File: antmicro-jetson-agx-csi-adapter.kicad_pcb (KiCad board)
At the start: 4 copper layers, 73.6 x 41 mm, 102 parts, among them IC1 MAX1708EEE+, J1 QTH-060-03-L-D-A, J2 WE_68715014522_ONE-SIDE, J3 SM06B-SRSS-TB(LF)(SN), J4 WE_68715014022, J5 SM09B-SRSS-TB(LF)(SN), J6 61300611121, Q1 BSS138AKA, U1 NTS0102DP, U2 PCA9547BS,118, U3 BNO055

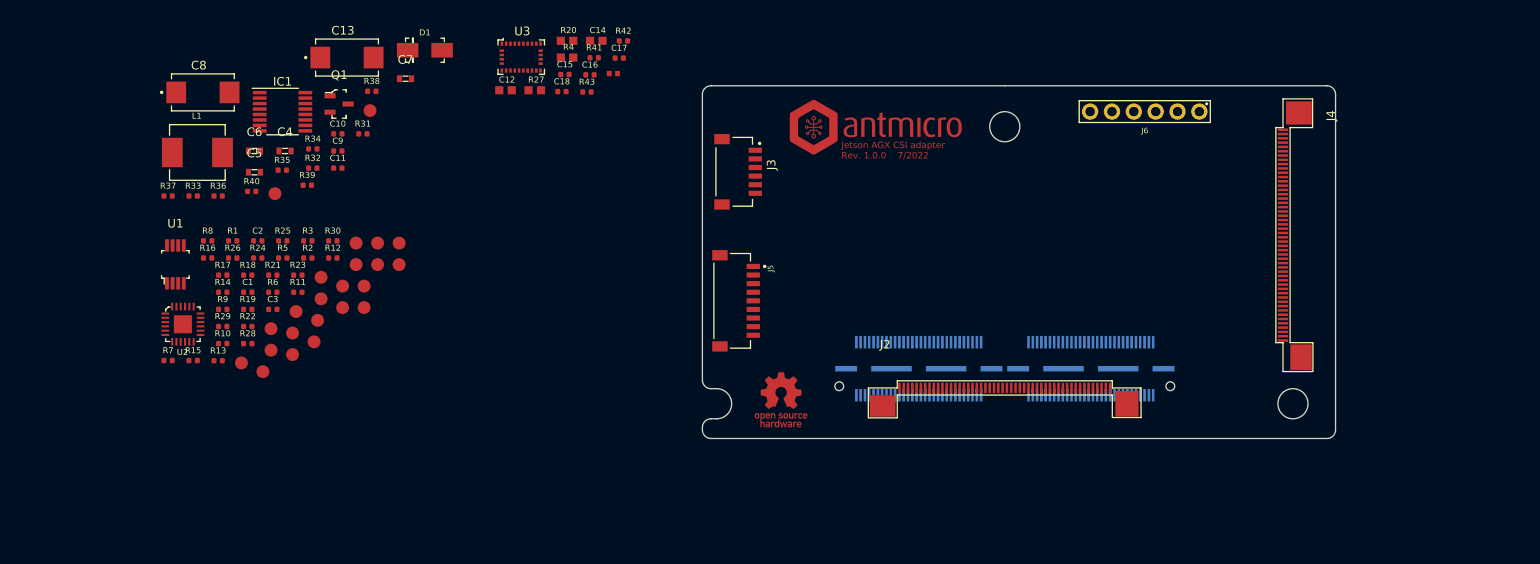
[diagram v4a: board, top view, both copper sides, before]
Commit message: Routed CSI interface
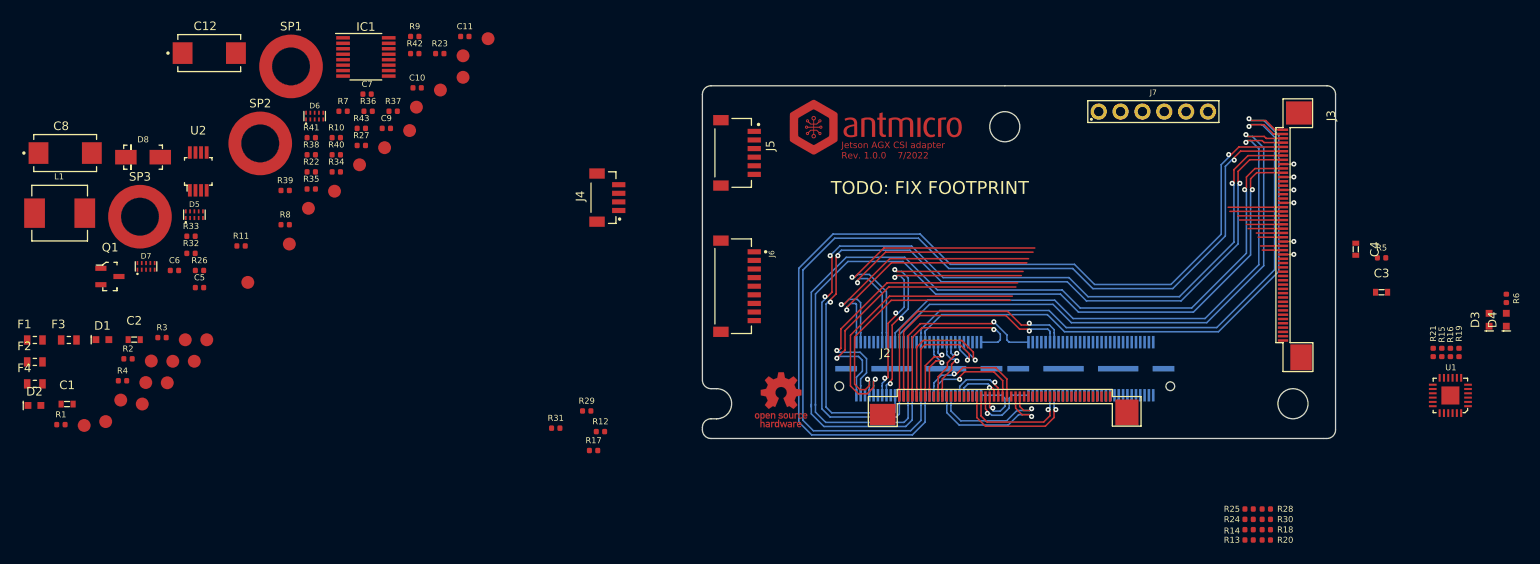
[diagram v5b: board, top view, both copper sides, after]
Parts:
- removed C13: C_220u_KEMET_D, antmicro-footprints:KEMET_D
- removed C14: 100n, antmicro-footprints:0603
- removed C15: C_10n_0402, antmicro-footprints:0402-cap
- removed C16, C17, C18: C_100n_0402, antmicro-footprints:0402-cap
- removed C19: 100n, antmicro-footprints:0402
- removed the J3 at (121.0, 78.0)
- removed U3: BNO055, antmicro-footprints:LGA-28_5.2x3.8mm_BNO0055
- added D2: LTST-C190GKT, antmicro-footprints:LED_0603, F.Cu at (37.2, 105.2)
- added D3: LTST-C190GKT, antmicro-footprints:LED_0603, F.Cu at (206.3, 95.2)
- added D4: LTST-C190GKT, antmicro-footprints:LED_0603, F.Cu at (208.3, 95.2)
- added D5: PUSB3F96X_PASS, antmicro-footprints:PUSB3F96X, F.Cu at (55.8, 83.0)
- added D6: PUSB3F96X_PASS, antmicro-footprints:PUSB3F96X, F.Cu at (69.8, 71.5)
- added D7: PUSB3F96X_PASS, antmicro-footprints:PUSB3F96X, F.Cu at (50.2, 89.0)
- added D8: B340A-13-F, antmicro-footprints:DO-214AC, F.Cu at (49.8, 76.3)
- added F1: 04671.25NR, antmicro-footprints:0603-Fuse-Littelfuse-0467, F.Cu at (37.2, 97.5)
- added F2: 04671.25NR, antmicro-footprints:0603-Fuse-Littelfuse-0467, F.Cu at (37.2, 100.1)
- added F3: 04671.25NR, antmicro-footprints:0603-Fuse-Littelfuse-0467, F.Cu at (41.2, 97.5)
- added F4: 04671.25NR, antmicro-footprints:0603-Fuse-Littelfuse-0467, F.Cu at (37.2, 102.7)
- added J4: BM04B-SRSS-TB-LF-SN, antmicro-footprints:BM04B-SRSS-TB-LF-SN, F.Cu at (103.8, 81.0)
- added J7: 61300611121, antmicro-footprints:61300611121, F.Cu at (167.3, 71.0)
- added SP1: 9774110360, antmicro-footprints:Mounting_Wuerth_WA-SMSI-M3_H11mm_9774110360, F.Cu at (67.0, 65.8)
- added SP2: 9774110360, antmicro-footprints:Mounting_Wuerth_WA-SMSI-M3_H11mm_9774110360, F.Cu at (63.5, 74.7)
- added SP3: 9774110360, antmicro-footprints:Mounting_Wuerth_WA-SMSI-M3_H11mm_9774110360, F.Cu at (49.5, 83.2)
- C1, C2, C3: value C_100n_0402 -> C_1u_0603; footprint antmicro-footprints:0402-cap -> antmicro-footprints:0603-cap
- C12: value 100n -> C_220u_KEMET_D; footprint antmicro-footprints:0603 -> antmicro-footprints:KEMET_D
- C5, C6, C7: value C_1u_0603 -> C_100n_0402; footprint antmicro-footprints:0603-cap -> antmicro-footprints:0402-cap
- D1: value B340A-13-F -> LTST-C190GKT; footprint antmicro-footprints:DO-214AC -> antmicro-footprints:LED_0603
- J5: value SM09B-SRSS-TB(LF)(SN) -> SM06B-SRSS-TB(LF)(SN); footprint antmicro-footprints:JST_SM09B-SRSS-TB(LF)(SN) -> antmicro-footprints:JST_SM06B-SRSS-TB(LF)(SN)
- J6: value 61300611121 -> SM09B-SRSS-TB(LF)(SN); footprint antmicro-footprints:61300611121 -> antmicro-footprints:JST_SM09B-SRSS-TB(LF)(SN)
- R10, R26, R37, R39, R9: value R_2k_0402 -> R_0R_0402
- R11: value R_0R_0402 -> R_10k_0402
- R12, R33, R34, R35: value R_0R_0402 -> R_2k_0402
- R15, R16: value R_2k2_0402 -> R_0R_0402
- R20: value 2k2 -> R_2k_0402; footprint antmicro-footprints:0603 -> antmicro-footprints:0402-res
- R22, R23: value R_0R_0402 -> R_2k2_0402
- R27: value 0R -> R_0R_0402; footprint antmicro-footprints:0603 -> antmicro-footprints:0402-res
- R3, R5: value R_0R_0402 -> R_200R_0402
- R38: value R_2R_0402 -> R_0R_0402
- R4: value 0R -> R_470R_0402; footprint antmicro-footprints:0603 -> antmicro-footprints:0402-res
- R40: value R_0R_0402 -> R_2R_0402
- R41, R43: value R_10k_0402 -> R_2k_0402
- R6: value R_0R_0402 -> R_470R_0402
- R8: value R_10k_0402 -> R_0R_0402
- U1: value NTS0102DP -> PCA9547BS,118; footprint antmicro-footprints:TSSOP-8_W3mm -> antmicro-footprints:HVQFN24
- U2: value PCA9547BS,118 -> NTS0102DP; footprint antmicro-footprints:HVQFN24 -> antmicro-footprints:TSSOP-8_W3mm
- moved U1 149.0 mm to (201.8, 104.0), turned to 180 degrees
- moved R15 145.2 mm to (200.8, 99.0), turned to -90 degrees
- moved R16 144.9 mm to (201.8, 99.0), turned to -90 degrees
- moved R6 143.4 mm to (208.3, 92.7), turned to -90 degrees
- moved R19 140.9 mm to (202.8, 99.0), turned to 90 degrees
- moved R21 135.2 mm to (199.8, 99.0), turned to 90 degrees
- moved C3 128.9 mm to (193.8, 92.0)
- moved R5 127.7 mm to (193.8, 88.0)
- moved C4 125.0 mm to (190.8, 87.0), turned to -90 degrees
- moved R14 122.5 mm to (178.4, 119.6)
- moved R18 122.0 mm to (180.4, 119.6)
- moved R13 121.6 mm to (178.4, 120.8)
- moved R28 120.0 mm to (180.4, 117.2)
- moved R24 119.2 mm to (178.4, 118.4)
- moved R25 116.6 mm to (178.4, 117.2)
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- renumbered J4 to J3
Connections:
- net /Cameras/CAM1_RST_3V3 renamed /Interface/CAM1_RST_3V3
- net /Cameras/CAM_RST_3V3 renamed /Interface/CAM_RST_3V3
- net CSI0_D1_N renamed /Interface/CSI0_D1_N
- net CSI0_D1_P renamed /Interface/CSI0_D1_P
- net CSI1_CLK_N renamed /Interface/CSI1_CLK_N
- net CSI1_D1_N renamed /Interface/CSI1_D1_N
- net CSI1_D1_P renamed /Interface/CSI1_D1_P
- net CSI2_CLK_N renamed /Interface/CSI2_CLK_N
- net CSI2_CLK_P renamed /Interface/CSI2_CLK_P
- net CSI2_D0_N renamed /Interface/CSI2_D0_N
- net CSI2_D0_P renamed /Interface/CSI2_D0_P
- net CSI2_D1_N renamed /Interface/CSI2_D1_N
- net CSI2_D1_P renamed /Interface/CSI2_D1_P
- net CSI3_CLK_N renamed /Interface/CSI3_CLK_N
- net CSI3_CLK_P renamed /Interface/CSI3_CLK_P
- net CSI3_D0_N renamed /Interface/CSI3_D0_N
- net CSI3_D0_P renamed /Interface/CSI3_D0_P
- net CSI3_D1_N renamed /Interface/CSI3_D1_N
- net CSI3_D1_P renamed /Interface/CSI3_D1_P
- net CSI4_D0_N renamed /Interface/CSI4_D0_N
- net CSI4_D0_P renamed /Interface/CSI4_D0_P
- net CSI4_D1_N renamed /Interface/CSI4_D1_N
- net CSI4_D1_P renamed /Interface/CSI4_D1_P
- net CSI5_CLK_N renamed /Interface/CSI5_CLK_N
- net CSI5_CLK_P renamed /Interface/CSI5_CLK_P
- net CSI5_D0_N renamed /Interface/CSI5_D0_N
- net CSI5_D0_P renamed /Interface/CSI5_D0_P
- net CSI5_D1_N renamed /Interface/CSI5_D1_N
- net CSI5_D1_P renamed /Interface/CSI5_D1_P
- net CSI6_CLK_N renamed /Interface/CSI6_CLK_N
- net CSI6_CLK_P renamed /Interface/CSI6_CLK_P
- net CSI6_D0_N renamed /Interface/CSI6_D0_N
- net CSI6_D0_P renamed /Interface/CSI6_D0_P
- net CSI6_D1_N renamed /Interface/CSI6_D1_N
- net CSI6_D1_P renamed /Interface/CSI6_D1_P
- net CSI7_CLK_N renamed /Interface/CSI7_CLK_N
- net CSI7_CLK_P renamed /Interface/CSI7_CLK_P
- net CSI7_D0_N renamed /Interface/CSI7_D0_N
- net CSI7_D0_P renamed /Interface/CSI7_D0_P
- net CSI7_D1_N renamed /Interface/CSI7_D1_N
- net CSI7_D1_P renamed /Interface/CSI7_D1_P
- C1 pad 1: +1V8 -> Net-(C1-Pad1)
- C12 pad 1: GND -> Net-(C12-Pad1)
- C12 pad 2: 3V3 -> GND
- C2 pad 1: +3V3 -> Net-(C2-Pad1)
- C3 pad 1: +3V3 -> Net-(C3-Pad1)
- C4 pad 1: +5V -> Net-(C4-Pad1)
- C6 pad 1: +5V -> +1V8
- IC1 pad 3: Net-(D1-PadA) -> Net-(D8-PadA)
- IC1 pad 4: Net-(D1-PadA) -> Net-(D8-PadA)
- IC1 pad 5: Net-(D1-PadA) -> Net-(D8-PadA)
- J1 pad 43: CSI4_CLK_P -> /Interface/CSI4_CLK_P
- J1 pad 45: CSI4_CLK_N -> /Interface/CSI4_CLK_N
- J1 pad 75: /Interface/I2C_GP3_CLK -> I2C_GP3_CLK
- J1 pad 77: /Interface/I2C_GP3_DAT -> I2C_GP3_DAT
- J2 pad 28: CSI4_CLK_N -> /Interface/CSI4_CLK_P
- J2 pad 29: CSI4_CLK_P -> /Interface/CSI4_CLK_N
- J2 pad 32: /Cameras/VSYNC_CAM0_3V3 -> /Interface/VSYNC_CAM0_3V3
- J2 pad 34: /Cameras/VSYNC_CAM1_3V3 -> /Interface/VSYNC_CAM1_3V3
- J2 pad 47: +3V3 -> Net-(C1-Pad1)
- J2 pad 48: +3V3 -> Net-(C1-Pad1)
- J2 pad 49: +5V -> Net-(C2-Pad1)
- J2 pad 50: +5V -> Net-(C2-Pad1)
- J3 pad 21: CSI1_D0_N -> /Interface/CSI1_D0_N
- J3 pad 22: CSI1_D0_P -> /Interface/CSI1_D0_P
- J3 pad 25: CSI0_D0_N -> /Interface/CSI0_D0_N
- J3 pad 26: CSI0_D0_P -> /Interface/CSI0_D0_P
- J3 pad 28: CSI0_CLK_N -> /Interface/CSI0_CLK_N
- J3 pad 29: CSI0_CLK_P -> /Interface/CSI0_CLK_P
- J3 pad 32: /Cameras/VSYNC_CAM3_3V3 -> /Interface/VSYNC_CAM3_3V3
- J3 pad 34: /Cameras/VSYNC_CAM2_3V3 -> /Interface/VSYNC_CAM2_3V3
- J3 pad 47: +3V3 -> Net-(C3-Pad1)
- J3 pad 48: +3V3 -> Net-(C3-Pad1)
- J3 pad 49: +5V -> Net-(C4-Pad1)
- J3 pad 50: +5V -> Net-(C4-Pad1)
- J5 pad 1: /Cameras/GPIO3 -> +5V
- J5 pad 2: /Cameras/GPIO4 -> GND
- J5 pad 3: /Cameras/GPIO5 -> CAM3_SDA
- J5 pad 4: /Cameras/GPIO6 -> CAM3_SCL
- J5 pad 5: /Cameras/DEPTH_CAM_SYNC -> unconnected-(J5-Pad5)
- J5 pad 6: /Cameras/LASER_PWM0 -> unconnected-(J5-Pad6)
- J6 pad 1: GND -> /Auxiliary/GPIO3
- J6 pad 2: /Cameras/DEPTH_CAM_SYNC_3V3 -> /Auxiliary/GPIO4
- J6 pad 3: /Cameras/VSYNC_CAM3_3V3 -> /Auxiliary/GPIO5
- J6 pad 4: /Cameras/VSYNC_CAM2_3V3 -> /Auxiliary/GPIO6
- J6 pad 5: /Cameras/VSYNC_CAM1_3V3 -> /Auxiliary/DEPTH_CAM_SYNC
- J6 pad 6: /Cameras/VSYNC_CAM0_3V3 -> /Auxiliary/LASER_PWM0
- L1 pad 2: Net-(D1-PadA) -> Net-(D8-PadA)
- Q1 pad 1: /Cameras/DEPTH_CAM_SYNC -> /Auxiliary/DEPTH_CAM_SYNC
- Q1 pad 3: /Cameras/DEPTH_CAM_SYNC_3V3 -> /Auxiliary/DEPTH_CAM_SYNC_3V3
- R10 pad 1: /Interface/SCL_3V3 -> /Auxiliary/SCL_3V3
- R10 pad 2: +3V3 -> Net-(R10-Pad2)
- R11 pad 2: CAM0_SDA -> +3V3
- R12 pad 1: Net-(R12-Pad1) -> /Auxiliary/AUX_I2C_SDA
- R12 pad 2: CAM0_SCL -> +3V3
- R13 pad 2: CAM2_SDA -> CAM0_SDA
- R14 pad 2: CAM2_SCL -> CAM0_SCL
- R15 pad 1: /Interface/MISC_I2C_SDA -> Net-(R15-Pad1)
- R15 pad 2: +3V3 -> CAM2_SDA
- R16 pad 1: +3V3 -> Net-(R16-Pad1)
- R16 pad 2: /Interface/MISC_I2C_SCL -> CAM2_SCL
- R17 pad 1: CAM0_SCL -> /Auxiliary/AUX_I2C_SCL
- R18 pad 1: CAM2_SCL -> CAM0_SCL
- R19 pad 1: CAM0_SDA -> CAM2_SCL
- R20 pad 1: Net-(IC6-Pad13) -> CAM0_SDA
- R20 pad 2: 3V3 -> +3V3
- R22 pad 1: Net-(R22-Pad1) -> /Auxiliary/MISC_I2C_SDA
- R22 pad 2: CAM1_SDA -> +3V3
- R23 pad 1: Net-(R23-Pad1) -> +3V3
- R23 pad 2: CAM1_SCL -> /Auxiliary/MISC_I2C_SCL
- R24 pad 2: CAM3_SDA -> CAM1_SDA
- R25 pad 2: CAM3_SCL -> CAM1_SCL
- R26 pad 1: CAM1_SCL -> Net-(R26-Pad1)
- R26 pad 2: +3V3 -> CAM3_SDA
- R27 pad 1: GND -> Net-(R27-Pad1)
- R27 pad 2: Net-(IC5-Pad7) -> CAM3_SCL
- R28 pad 1: CAM3_SCL -> CAM1_SCL
- R29 pad 1: CAM1_SDA -> CAM3_SCL
- R3 pad 1: Net-(R3-Pad1) -> Net-(C1-Pad1)
- R3 pad 2: +3V3 -> Net-(D1-Pad1)
- R30 pad 1: CAM3_SDA -> CAM1_SDA
- R31 pad 1: Net-(IC1-Pad1) -> CAM3_SDA
- R32 pad 1: Net-(IC1-Pad2) -> /Auxiliary/SDA_3V3
- R33 pad 1: /Cameras/VSYNC_CAM0_3V3 -> /Auxiliary/SCL_3V3
- R33 pad 2: /Cameras/DEPTH_CAM_SYNC_3V3 -> +3V3
- R34 pad 1: /Cameras/VSYNC_CAM1_3V3 -> Net-(IC1-Pad1)
- R34 pad 2: /Cameras/DEPTH_CAM_SYNC_3V3 -> +3V3
- R35 pad 1: /Cameras/VSYNC_CAM2_3V3 -> Net-(IC1-Pad2)
- R35 pad 2: /Cameras/DEPTH_CAM_SYNC_3V3 -> +3V3
- R36 pad 1: /Cameras/VSYNC_CAM3_3V3 -> /Auxiliary/VSYNC_CAM0_3V3
- R36 pad 2: /Cameras/DEPTH_CAM_SYNC_3V3 -> /Auxiliary/DEPTH_CAM_SYNC_3V3
- R37 pad 1: /Cameras/DEPTH_CAM_SYNC_3V3 -> /Auxiliary/VSYNC_CAM1_3V3
- R37 pad 2: +3V3 -> /Auxiliary/DEPTH_CAM_SYNC_3V3
- R38 pad 1: Net-(C11-Pad1) -> /Auxiliary/VSYNC_CAM2_3V3
- R38 pad 2: Net-(C13-Pad1) -> /Auxiliary/DEPTH_CAM_SYNC_3V3
- R39 pad 1: GND -> /Auxiliary/VSYNC_CAM3_3V3
- R39 pad 2: /Cameras/DEPTH_CAM_SYNC -> /Auxiliary/DEPTH_CAM_SYNC_3V3
- R4 pad 1: Net-(IC5-Pad7) -> Net-(C2-Pad1)
- R4 pad 2: 3V3 -> Net-(D2-Pad1)
- R40 pad 1: Net-(C13-Pad1) -> Net-(C11-Pad1)
- R40 pad 2: +5V -> Net-(C12-Pad1)
- R41 pad 1: Net-(R41-Pad1) -> /Auxiliary/DEPTH_CAM_SYNC_3V3
- R42 pad 1: Net-(R41-Pad1) -> Net-(C12-Pad1)
- R42 pad 2: GND -> +5V
- R43 pad 1: Net-(R43-Pad1) -> GND
- R43 pad 2: +3V3 -> /Auxiliary/DEPTH_CAM_SYNC
- R5 pad 1: GND -> Net-(C3-Pad1)
- R5 pad 2: Net-(R3-Pad1) -> Net-(D3-Pad1)
- R6 pad 1: /Interface/SDA_3V3 -> Net-(C4-Pad1)
- R6 pad 2: Net-(R6-Pad2) -> Net-(D4-Pad1)
- R7 pad 1: /Interface/SCL_3V3 -> Net-(R7-Pad1)
- R7 pad 2: Net-(R7-Pad2) -> +3V3
- R8 pad 1: Net-(R8-Pad1) -> GND
- R8 pad 2: +3V3 -> Net-(R7-Pad1)
- R9 pad 1: /Interface/SDA_3V3 -> /Auxiliary/SDA_3V3
- R9 pad 2: +3V3 -> Net-(R9-Pad2)
- TP12 pad 1: /Interface/I2C_GP3_DAT -> CAM0_SDA
- TP13 pad 1: /Interface/I2C_GP3_CLK -> CAM0_SCL
- TP14 pad 1: CAM0_SDA -> CAM2_SDA
- TP15 pad 1: CAM0_SCL -> CAM2_SCL
- TP16 pad 1: CAM2_SDA -> CAM1_SDA
- TP17 pad 1: CAM2_SCL -> CAM1_SCL
- TP18 pad 1: CAM1_SDA -> CAM3_SDA
- TP19 pad 1: CAM1_SCL -> CAM3_SCL
- TP20 pad 1: CAM3_SDA -> /Auxiliary/I2C_GP3_DAT
- TP21 pad 1: CAM3_SCL -> /Auxiliary/I2C_GP3_CLK
- TP22 pad 1: /Cameras/DEPTH_CAM_SYNC_3V3 -> /Auxiliary/DEPTH_CAM_SYNC_3V3
- U1 pad 1: /Interface/SCL_3V3 -> Net-(R13-Pad1)
- U1 pad 2: GND -> Net-(R14-Pad1)
- U1 pad 3: +1V8 -> Net-(R24-Pad1)
- U1 pad 4: /Interface/I2C_GP3_CLK -> Net-(R25-Pad1)
- U1 pad 5: /Interface/I2C_GP3_DAT -> Net-(R15-Pad1)
- U1 pad 6: +1V8 -> Net-(R16-Pad1)
- U1 pad 7: +3V3 -> Net-(R26-Pad1)
- U1 pad 8: /Interface/SDA_3V3 -> Net-(R27-Pad1)
- U2 pad 1: Net-(R11-Pad1) -> /Auxiliary/SCL_3V3
- U2 pad 2: Net-(R12-Pad1) -> GND
- U2 pad 3: Net-(R22-Pad1) -> +1V8
- U2 pad 4: Net-(R23-Pad1) -> /Auxiliary/I2C_GP3_CLK
- U2 pad 5: Net-(R13-Pad1) -> /Auxiliary/I2C_GP3_DAT
- U2 pad 6: Net-(R14-Pad1) -> +1V8
- U2 pad 7: Net-(R24-Pad1) -> +3V3
- U2 pad 8: Net-(R25-Pad1) -> /Auxiliary/SDA_3V3
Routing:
- net /Interface/CSI2_D1_N: track 0.00 -> 108.8 mm, vias 0 -> 1
- net /Interface/CSI2_D1_P: track 0.00 -> 106.4 mm, vias 0 -> 1
- net /Interface/CSI2_CLK_N: track 0.00 -> 101.0 mm, vias 0 -> 1
- net /Interface/CSI2_CLK_P: track 0.00 -> 98.5 mm, vias 0 -> 1
- net /Interface/CSI2_D0_N: track 0.00 -> 98.3 mm, vias 0 -> 3
- net /Interface/CSI2_D0_P: track 0.00 -> 95.7 mm, vias 0 -> 3
- net /Interface/CSI3_D1_N: track 0.00 -> 71.5 mm, vias 0 -> 1
- net /Interface/CSI3_D1_P: track 0.00 -> 70.7 mm, vias 0 -> 1
- net /Interface/CSI3_D0_N: track 0.00 -> 69.2 mm, vias 0 -> 1
- net /Interface/CSI3_D0_P: track 0.00 -> 68.4 mm, vias 0 -> 1
- net /Interface/CSI1_D1_N: track 0.00 -> 39.9 mm, vias 0 -> 1
- net /Interface/CSI1_D1_P: track 0.00 -> 37.9 mm, vias 0 -> 1
- net /Interface/CSI0_D0_N: track 0.00 -> 37.1 mm, vias 0 -> 1
- net /Interface/CSI1_D0_N: track 0.00 -> 36.5 mm, vias 0 -> 1
- net /Interface/CSI0_D1_N: track 0.00 -> 36.3 mm, vias 0 -> 3
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- added copper zone on In1.Cu, net GND
- added copper zone on In2.Cu, net GND
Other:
- board text added: "TODO: FIX FOOTPRINT"

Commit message: Routed I2C signals, completed a layout of the voltage converter and I2C IC.
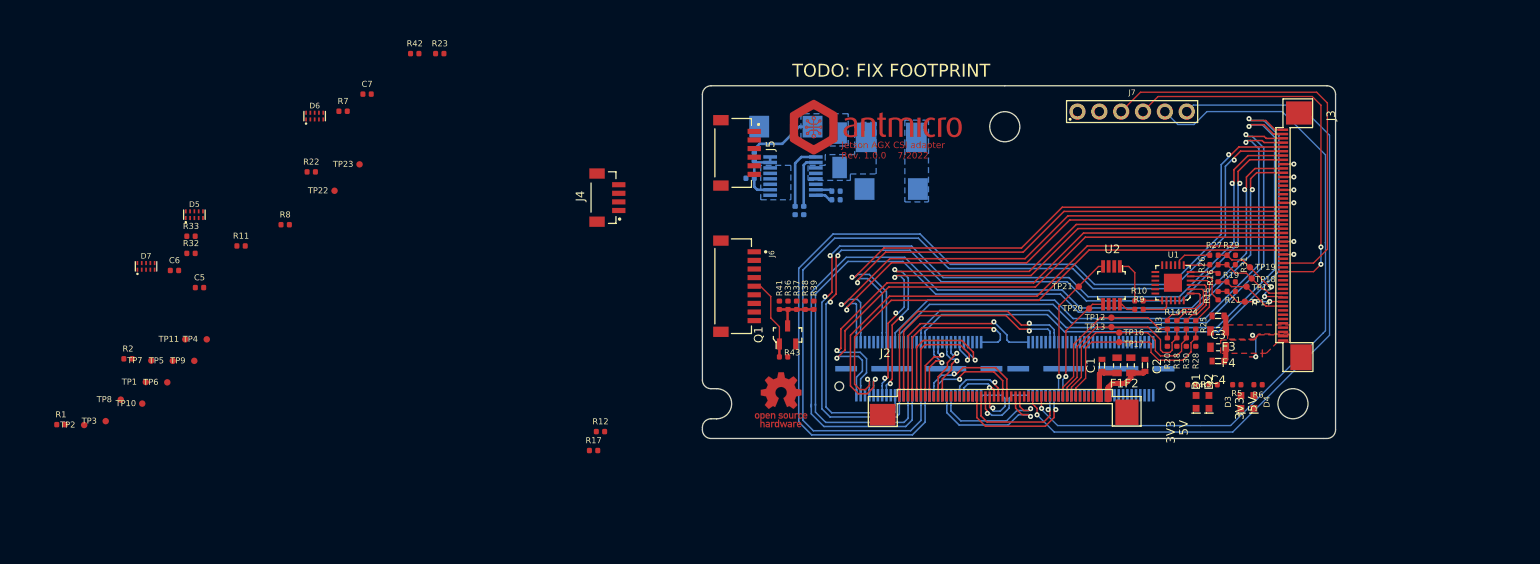
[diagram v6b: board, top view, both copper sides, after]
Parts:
- removed SP1, SP2, SP3: 9774110360, antmicro-footprints:Mounting_Wuerth_WA-SMSI-M3_H11mm_9774110360
- C10, C11, C12, C8, C9, D8, IC1, L1, R34, R35, R40: moved to B.Cu
- TP1, TP10, TP11, TP12, TP13, TP14, TP15, TP16, TP17, TP18, TP19, TP2, TP20, TP21, TP22, TP23, TP3, TP4, TP5, TP6, TP7, TP8, TP9: value TP -> TP_SMD_0_75MM; footprint antmicro-footprints:TP-R-1.5 -> antmicro-footprints:Testpoint_smd_0_75mm
- moved F4 137.6 mm to (174.8, 98.4), turned to 180 degrees
- moved D2 136.5 mm to (173.7, 104.8), turned to 90 degrees
- moved F3 133.6 mm to (174.8, 96.5), turned to 180 degrees
- moved F2 127.4 mm to (164.7, 100.5), turned to 90 degrees
- moved D1 127.3 mm to (172.2, 104.8), turned to 90 degrees
- moved R4 126.8 mm to (174.2, 102.8), turned to 180 degrees
- moved F1 125.8 mm to (163.1, 100.5), turned to 90 degrees
- moved C1 120.4 mm to (161.3, 100.5), turned to 90 degrees
- moved R3 119.8 mm to (171.8, 102.8)
- moved R26 117.9 mm to (174.3, 88.8)
- moved C2 117.5 mm to (166.3, 100.5), turned to 90 degrees
- moved TP18 111.9 mm to (178.7, 90.5)
- moved TP15 109.4 mm to (178.1, 91.4)
- moved U2 107.0 mm to (162.4, 91.2), turned to 180 degrees
- moved TP16 101.5 mm to (163.3, 96.8)
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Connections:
- net Net-(C1-Pad1) renamed /Interface/3V3_FFC_B
- net Net-(C12-Pad1) renamed /Auxiliary/5V_C
- net Net-(C2-Pad1) renamed /Interface/5V_FFC_B
- net Net-(C3-Pad1) renamed /Interface/3V3_FFC_S
- net Net-(C4-Pad1) renamed /Interface/5V_FFC_S
- D7 pad 1: /Auxiliary/VSYNC_CAM0_3V3 -> VSYNC_CAM0_3V3
- D7 pad 10: /Auxiliary/VSYNC_CAM0_3V3 -> VSYNC_CAM0_3V3
- D7 pad 2: /Auxiliary/VSYNC_CAM1_3V3 -> VSYNC_CAM1_3V3
- D7 pad 4: /Auxiliary/VSYNC_CAM2_3V3 -> VSYNC_CAM2_3V3
- D7 pad 5: /Auxiliary/VSYNC_CAM3_3V3 -> VSYNC_CAM3_3V3
- D7 pad 6: /Auxiliary/VSYNC_CAM3_3V3 -> VSYNC_CAM3_3V3
- D7 pad 7: /Auxiliary/VSYNC_CAM2_3V3 -> VSYNC_CAM2_3V3
- D7 pad 9: /Auxiliary/VSYNC_CAM1_3V3 -> VSYNC_CAM1_3V3
- J2 pad 32: /Interface/VSYNC_CAM0_3V3 -> VSYNC_CAM0_3V3
- J2 pad 34: /Interface/VSYNC_CAM1_3V3 -> VSYNC_CAM1_3V3
- J3 pad 32: /Interface/VSYNC_CAM3_3V3 -> VSYNC_CAM3_3V3
- J3 pad 34: /Interface/VSYNC_CAM2_3V3 -> VSYNC_CAM2_3V3
- J7 pad 3: /Auxiliary/VSYNC_CAM3_3V3 -> VSYNC_CAM3_3V3
- J7 pad 4: /Auxiliary/VSYNC_CAM2_3V3 -> VSYNC_CAM2_3V3
- J7 pad 5: /Auxiliary/VSYNC_CAM1_3V3 -> VSYNC_CAM1_3V3
- J7 pad 6: /Auxiliary/VSYNC_CAM0_3V3 -> VSYNC_CAM0_3V3
- R36 pad 1: /Auxiliary/VSYNC_CAM0_3V3 -> VSYNC_CAM0_3V3
- R37 pad 1: /Auxiliary/VSYNC_CAM1_3V3 -> VSYNC_CAM1_3V3
- R38 pad 1: /Auxiliary/VSYNC_CAM2_3V3 -> VSYNC_CAM2_3V3
- R39 pad 1: /Auxiliary/VSYNC_CAM3_3V3 -> VSYNC_CAM3_3V3
- TP20 pad 1: /Auxiliary/I2C_GP3_DAT -> I2C_GP3_DAT
- TP21 pad 1: /Auxiliary/I2C_GP3_CLK -> I2C_GP3_CLK
- U2 pad 4: /Auxiliary/I2C_GP3_CLK -> I2C_GP3_CLK
- U2 pad 5: /Auxiliary/I2C_GP3_DAT -> I2C_GP3_DAT
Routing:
- net VSYNC_CAM0_3V3: track 0.00 -> 83.4 mm, vias 0 -> 1
- net VSYNC_CAM1_3V3: track 0.00 -> 82.3 mm, vias 0 -> 1
- net VSYNC_CAM3_3V3: track 0.00 -> 48.2 mm
- net VSYNC_CAM2_3V3: track 0.00 -> 45.1 mm, vias 0 -> 2
- net /Interface/CSI0_CLK_P: track 32.8 -> 64.4 mm
- net /Interface/CSI0_CLK_N: track 35.6 -> 66.8 mm
- net /Interface/CSI0_D0_P: track 36.1 -> 66.6 mm
- net /Interface/CSI0_D0_N: track 37.1 -> 67.2 mm
- net /Interface/CSI0_D1_P: track 35.1 -> 63.7 mm
- net /Interface/CSI0_D1_N: track 36.3 -> 64.5 mm
- net /Interface/CSI1_D0_P: track 34.5 -> 61.3 mm
- net /Interface/CSI1_D0_N: track 36.5 -> 62.9 mm
- net /Interface/CSI1_D1_P: track 37.9 -> 62.7 mm
- net /Interface/CSI1_D1_N: track 39.9 -> 64.3 mm
- net CAM1_SDA: track 0.00 -> 23.4 mm
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- added copper zone on B.Cu, net +3V3
- added copper zone on B.Cu, net /Auxiliary/5V_C
- added copper zone on F.Cu, net /Interface/3V3_FFC_S
- added copper zone on F.Cu, net /Interface/5V_FFC_S
- added copper zone on B.Cu, net GND
- added copper zone on B.Cu, net Net-(D8-PadA)
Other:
- board text added: "3V3"
- board text added: "5V"

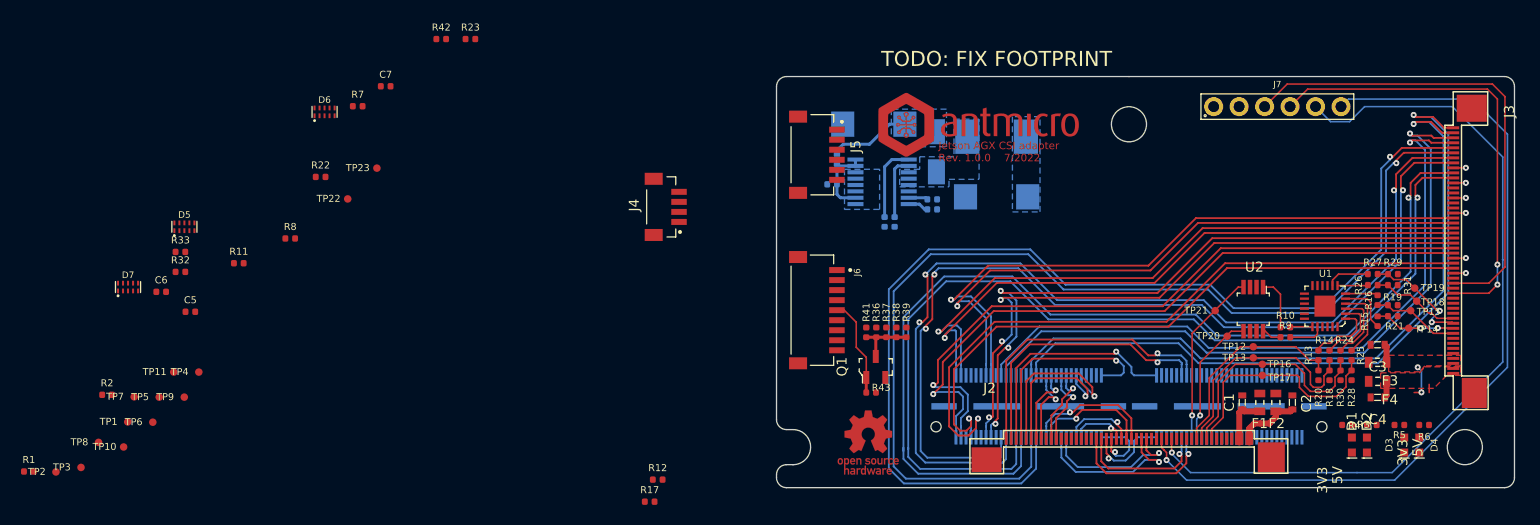
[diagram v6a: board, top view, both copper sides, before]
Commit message: Finished layout of most of the other signals, rerouted CSI
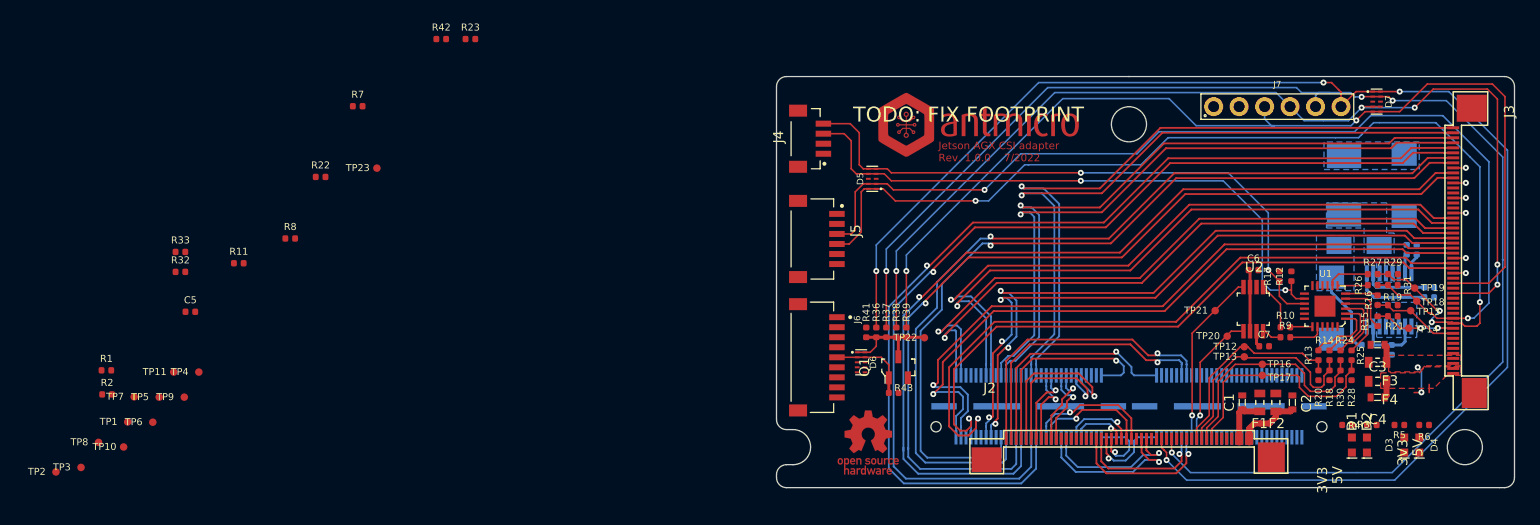
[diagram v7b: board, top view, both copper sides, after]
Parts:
- moved D7 125.9 mm to (174.7, 70.5), turned to -90 degrees
- moved C6 109.0 mm to (162.4, 87.3)
- moved C7 91.4 mm to (163.5, 94.9)
- moved D5 68.8 mm to (124.4, 78.2), turned to 90 degrees
- moved R17 66.7 mm to (165.0, 87.9), turned to 90 degrees
- moved R12 66.4 mm to (166.2, 87.9), turned to 90 degrees
- moved TP22 59.2 mm to (129.6, 94.1)
- moved D6 59.1 mm to (123.3, 96.5), turned to -90 degrees
- moved C11 58.2 mm to (176.2, 95.3), turned to -90 degrees
- moved R40 56.0 mm to (173.7, 94.8), turned to 180 degrees
- moved R34 54.8 mm to (179.9, 90.0), turned to 0 degrees
- moved R35 53.7 mm to (179.9, 89.0), turned to 0 degrees
- moved IC1 51.9 mm to (175.9, 90.3), turned to -90 degrees
- moved C12 49.2 mm to (170.2, 91.1), turned to -90 degrees
- moved C10 48.5 mm to (178.7, 85.3), turned to -90 degrees
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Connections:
- D5 pad 4: /Auxiliary/AUX_I2C_SCL -> /Auxiliary/AUX_I2C_SDA
- D5 pad 5: /Auxiliary/AUX_I2C_SDA -> /Auxiliary/AUX_I2C_SCL
- D5 pad 6: /Auxiliary/AUX_I2C_SDA -> /Auxiliary/AUX_I2C_SCL
- D5 pad 7: /Auxiliary/AUX_I2C_SCL -> /Auxiliary/AUX_I2C_SDA
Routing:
- net CAM3_SDA: track 8.93 -> 101.8 mm, vias 0 -> 2
- net CAM3_SCL: track 11.4 -> 104.2 mm, vias 2 -> 4
- net VSYNC_CAM0_3V3: track 83.4 -> 146.2 mm, vias 1 -> 4
- net /Auxiliary/AUX_I2C_SCL: track 0.00 -> 61.5 mm, vias 0 -> 2
- net /Auxiliary/AUX_I2C_SDA: track 0.00 -> 61.2 mm, vias 0 -> 2
- net VSYNC_CAM1_3V3: track 82.3 -> 141.8 mm, vias 1 -> 4
- net VSYNC_CAM2_3V3: track 45.1 -> 102.2 mm, vias 2 -> 5
- net VSYNC_CAM3_3V3: track 48.2 -> 102.1 mm, vias 0 -> 2
- net /Interface/CSI2_D0_N: track 98.3 -> 87.0 mm, vias 3 -> 1
- net /Interface/CSI2_D0_P: track 95.7 -> 84.6 mm, vias 3 -> 1
- net /Interface/CSI2_D1_N: track 108.8 -> 98.2 mm
- net /Interface/CSI2_D1_P: track 106.4 -> 95.8 mm
- net /Interface/CSI2_CLK_P: track 98.5 -> 88.5 mm
- net /Interface/CSI2_CLK_N: track 101.0 -> 91.1 mm
- net +1V8: track 0.00 -> 6.16 mm
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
